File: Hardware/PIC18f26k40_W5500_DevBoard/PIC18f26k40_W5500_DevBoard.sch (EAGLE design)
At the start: 23 parts, among them J2 MAGJACK, U1 W5500, U2 PIC18F2523-I/SO

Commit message: Finished functional parts of Heep 18f26k40 board
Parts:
- added C15, C16: 15pF, SparkFun-Passives:CAP0603-CAP
- added C17: 100nF, SparkFun-Passives:CAP0603-CAP
- added C18, C19: 6.8nF, SparkFun-Passives:CAP0603-CAP
- added C20: 10nf, SparkFun-Passives:CAP0603-CAP
- added R10, R11, R8, R9: 51, SparkFun-Passives:RESISTOR0603-RES
- added R5: 4.7k, SparkFun-Passives:RESISTOR0603-RES
- added R6, R7: 330, SparkFun-Passives:RESISTOR0603-RES
- added Y1: (no value), SparkFun-Clocks:CRYSTALSMD-5X3.2-4PAD
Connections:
- new net ACTLED: J2.YLED-, U1.ACTLED
- new net LNKLED: J2.GLED-, U1.LINKLED
- new net MCLR: J1.6, R5.1, U2.~MCLR/VPP/RE3
- new net N$10: C19.2, J2.RD-
- new net N$11: C20.1, J2.RCT, R10.1, R11.1
- new net N$5: C15.1, U1.XO, Y1.2
- new net N$6: C16.1, U1.XI/CLKIN, Y1.1
- new net N$7: J2.YLED+, R6.2
- new net N$8: C18.2, J2.RD+
- new net N$9: J2.GLED+, R7.2
- new net PGC: J1.2, U2.RB6//KBI2/PGC
- new net PGD: J1.3, U2.RB7/KBI3/PGD
- new net PGM: J1.1
- new net RDN: C19.1, R11.2, U1.RXN
- new net RDP: C18.1, R10.2, U1.RXP
- new net TDN: J2.TD-, R9.1, U1.TXN
- new net TDP: J2.TD+, R8.1, U1.TXP
- net GND: now also C15.2, C16.2, C17.2, C20.2, J1.4, J2.SHIELD@0, J2.SHIELD@1, U1.AGND@1, U1.AGND@2, U1.AGND@3, U1.AGND@4, U1.AGND@5, U1.AGND@6, U1.RSVD@1, U1.RSVD@2, U1.RSVD@3, U1.RSVD@4, U1.RSVD@5, U1.RSVD@6
- net VCC: now also J1.5, R5.2, R6.1, R7.1, U1.PMODE0, U1.PMODE1, U1.PMODE2
- net VCCA: now also C17.1, J2.TCT, R8.2, R9.2, U1.AVDD@1, U1.AVDD@2, U1.AVDD@3, U1.AVDD@4, U1.AVDD@5, U1.AVDD@6
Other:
- moved on the sheet: C3, C5, R1

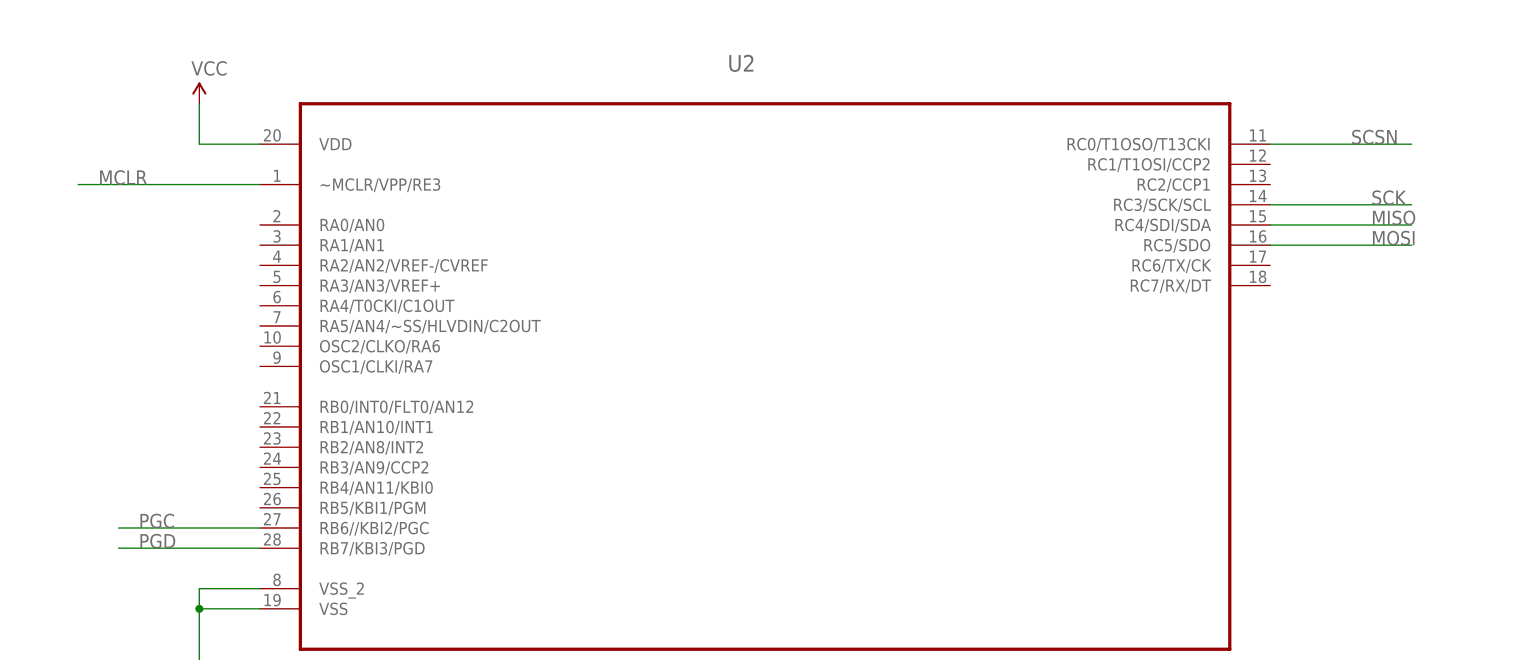
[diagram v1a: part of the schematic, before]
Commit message: #251 Labeled all PIC pins
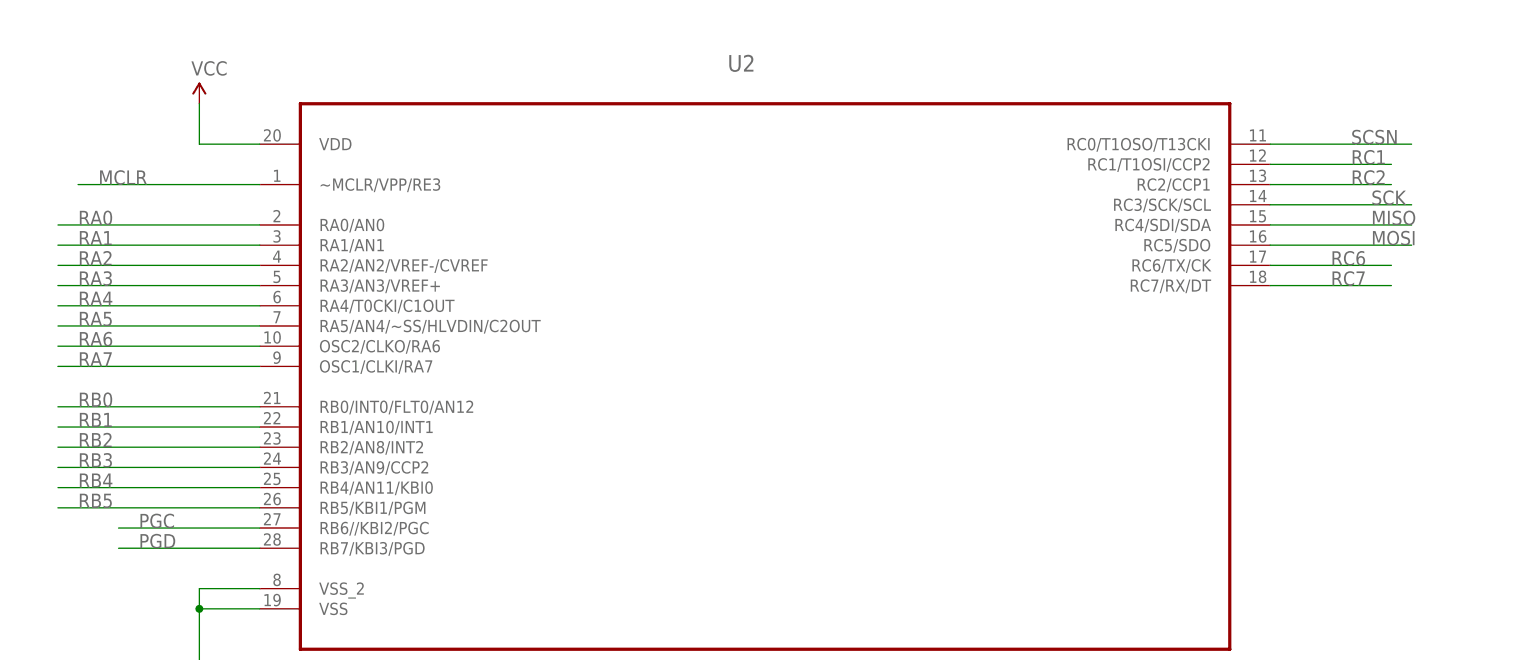
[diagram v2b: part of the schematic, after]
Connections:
- new net RA0: U2.RA0/AN0
- new net RA1: U2.RA1/AN1
- new net RA2: U2.RA2/AN2/VREF-/CVREF
- new net RA3: U2.RA3/AN3/VREF+
- new net RA4: U2.RA4/T0CKI/C1OUT
- new net RA5: U2.RA5/AN4/~SS/HLVDIN/C2OUT
- new net RA6: U2.OSC2/CLKO/RA6
- new net RA7: U2.OSC1/CLKI/RA7
- new net RB0: U2.RB0/INT0/FLT0/AN12
- new net RB1: U2.RB1/AN10/INT1
- new net RB2: U2.RB2/AN8/INT2
- new net RB3: U2.RB3/AN9/CCP2
- new net RB4: U2.RB4/AN11/KBI0
- new net RB5: U2.RB5/KBI1/PGM
- new net RC1: U2.RC1/T1OSI/CCP2
- new net RC2: U2.RC2/CCP1
- new net RC6: U2.RC6/TX/CK
- new net RC7: U2.RC7/RX/DT
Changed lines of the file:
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@@
+</segment>
+</net>
+<net name="RC1" class="0">
+<segment>
+<pinref part="U2" gate="A" pin="RC1/T1OSI/CCP2"/>
+<wire x1="116.84" y1="86.36" x2="132.08" y2="86.36" width="0.1524" layer="91"/>
+<label x="127" y="86.36" size="1.778" layer="95"/>
+</segment>
+</net>
+<net name="RC2" class="0">
+<segment>
+<pinref part="U2" gate="A" pin="RC2/CCP1"/>
+<wire x1="116.84" y1="83.82" x2="132.08" y2="83.82" width="0.1524" layer="91"/>
+<label x="127" y="83.82" size="1.778" layer="95"/>
+</segment>
+</net>
+<net name="RC6" class="0">
+<segment>
+<pinref part="U2" gate="A" pin="RC6/TX/CK"/>
+<wire x1="116.84" y1="73.66" x2="132.08" y2="73.66" width="0.1524" layer="91"/>
+<label x="124.46" y="73.66" size="1.778" layer="95"/>
+</segment>
+</net>
+<net name="RC7" class="0">
+<segment>
+<pinref part="U2" gate="A" pin="RC7/RX/DT"/>
+<wire x1="116.84" y1="71.12" x2="132.08" y2="71.12" width="0.1524" layer="91"/>
+<label x="124.46" y="71.12" size="1.778" layer="95"/>
+</segment>
+</net>
+<net name="RA0" class="0">
+<segment>
+<pinref part="U2" gate="A" pin="RA0/AN0"/>
+<wire x1="-10.16" y1="78.74" x2="-35.56" y2="78.74" width="0.1524" layer="91"/>
+<label x="-33.02" y="78.74" size="1.778" layer="95"/>
+</segment>
+</net>
+<net name="RA1" class="0">
+<segment>
+<pinref part="U2" gate="A" pin="RA1/AN1"/>
+<wire x1="-10.16" y1="76.2" x2="-35.56" y2="76.2" width="0.1524" layer="91"/>
+<label x="-33.02" y="76.2" size="1.778" layer="95"/>
+</segment>
+</net>
+<net name="RA2" class="0">
+<segment>
+<pinref part="U2" gate="A" pin="RA2/AN2/VREF-/CVREF"/>
+<wire x1="-10.16" y1="73.66" x2="-35.56" y2="73.66" width="0.1524" layer="91"/>
+<label x="-33.02" y="73.66" size="1.778" layer="95"/>
+</segment>
+</net>
+<net name="RA3" class="0">
+<segment>
+<pinref part="U2" gate="A" pin="RA3/AN3/VREF+"/>
+<wire x1="-10.16" y1="71.12" x2="-35.56" y2="71.12" width="0.1524" layer="91"/>
+<label x="-33.02" y="71.12" size="1.778" layer="95"/>
+</segment>
+</net>
+<net name="RA4" class="0">
+<segment>
+<pinref part="U2" gate="A" pin="RA4/T0CKI/C1OUT"/>
+<wire x1="-10.16" y1="68.58" x2="-35.56" y2="68.58" width="0.1524" layer="91"/>
+<label x="-33.02" y="68.58" size="1.778" layer="95"/>
+</segment>
+</net>
+<net name="RA5" class="0">
+<segment>
+<pinref part="U2" gate="A" pin="RA5/AN4/~SS/HLVDIN/C2OUT"/>
+<wire x1="-10.16" y1="66.04" x2="-35.56" y2="66.04" width="0.1524" layer="91"/>
+<label x="-33.02" y="66.04" size="1.778" layer="95"/>
+</segment>
+</net>
+<net name="RA6" class="0">
+<segment>
+<pinref part="U2" gate="A" pin="OSC2/CLKO/RA6"/>
+<wire x1="-10.16" y1="63.5" x2="-35.56" y2="63.5" width="0.1524" layer="91"/>
+<label x="-33.02" y="63.5" size="1.778" layer="95"/>
+</segment>
+</net>
+<net name="RA7" class="0">
+<segment>
+<pinref part="U2" gate="A" pin="OSC1/CLKI/RA7"/>
+<wire x1="-10.16" y1="60.96" x2="-35.56" y2="60.96" width="0.1524" layer="91"/>
+<label x="-33.02" y="60.96" size="1.778" layer="95"/>
+</segment>
+</net>
+<net name="RB0" class="0">
+<segment>
+<pinref part="U2" gate="A" pin="RB0/INT0/FLT0/AN12"/>
+<wire x1="-10.16" y1="55.88" x2="-35.56" y2="55.88" width="0.1524" layer="91"/>
+<label x="-33.02" y="55.88" size="1.778" layer="95"/>
+</segment>
+</net>
+<net name="RB1" class="0">
+<segment>
+<pinref part="U2" gate="A" pin="RB1/AN10/INT1"/>
+<wire x1="-10.16" y1="53.34" x2="-35.56" y2="53.34" width="0.1524" layer="91"/>
+<label x="-33.02" y="53.34" size="1.778" layer="95"/>
+</segment>
+</net>
+<net name="RB2" class="0">
+<segment>
+<pinref part="U2" gate="A" pin="RB2/AN8/INT2"/>
+<wire x1="-10.16" y1="50.8" x2="-35.56" y2="50.8" width="0.1524" layer="91"/>
+<label x="-33.02" y="50.8" size="1.778" layer="95"/>
+</segment>
+</net>
+<net name="RB3" class="0">
+<segment>
+<pinref part="U2" gate="A" pin="RB3/AN9/CCP2"/>
+<wire x1="-10.16" y1="48.26" x2="-35.56" y2="48.26" width="0.1524" layer="91"/>
+<label x="-33.02" y="48.26" size="1.778" layer="95"/>
+</segment>
+</net>
+<net name="RB4" class="0">
+<segment>
+<pinref part="U2" gate="A" pin="RB4/AN11/KBI0"/>
+<wire x1="-10.16" y1="45.72" x2="-35.56" y2="45.72" width="0.1524" layer="91"/>
+<label x="-33.02" y="45.72" size="1.778" layer="95"/>
+</segment>
+</net>
+<net name="RB5" class="0">
+<segment>
+<pinref part="U2" gate="A" pin="RB5/KBI1/PGM"/>
+<wire x1="-10.16" y1="43.18" x2="-35.56" y2="43.18" width="0.1524" layer="91"/>
+<label x="-33.02" y="43.18" size="1.778" layer="95"/>
 </segment>
 </net>
